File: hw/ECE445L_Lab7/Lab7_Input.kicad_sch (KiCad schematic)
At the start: 5 parts, among them SW1 UP, SW2 DOWN, SW3 LEFT, SW4 RIGHT, SW5 MODE

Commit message: work on schem
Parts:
- removed SW1: UP, ECE445L:SW_PUSH_6mm, symbol ECE445L:SW_Push
- removed SW2: DOWN, ECE445L:SW_PUSH_6mm, symbol ECE445L:SW_Push
- removed SW3: LEFT, ECE445L:SW_PUSH_6mm, symbol ECE445L:SW_Push
- removed SW4: RIGHT, ECE445L:SW_PUSH_6mm, symbol ECE445L:SW_Push
- removed SW5: MODE, ECE445L:SW_PUSH_6mm, symbol ECE445L:SW_Push
- added J2: Conn_01x08, symbol Connector_Generic:Conn_01x08
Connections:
- new net uC_{1} - PA0: J2.5 (Pin_5)
- new net uC_{1} - PA1: J2.6 (Pin_6)
- new net uC_{1} - PA11: J2.8 (Pin_8)
- new net uC_{1} - PA23: J2.3 (Pin_3)
- new net uC_{1} - PA26: J2.4 (Pin_4)
- new net uC_{1} - PA3: J2.7 (Pin_7)
- new net uC_{1} - PA4: J2.1 (Pin_1)
- new net uC_{1} - PA7: J2.2 (Pin_2)

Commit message: more updates
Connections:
- net uC_{1} - PA0 renamed uC_{1} - KC1
- net uC_{1} - PA1 renamed uC_{1} - KC2
- net uC_{1} - PA26 renamed uC_{1} - KR4
- net uC_{1} - PA4 renamed uC_{1} - KR1
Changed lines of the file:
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@@
 	(generator_version "10.0")
 	(paper "A4")
-	(global_label "uC_{1} - PA4"
+	(global_label "uC_{1} - KR1"
 		(shape output)
 		(at 87.63 40.005 180)
@@
 		)
 		(property "Intersheetrefs" "${INTERSHEET_REFS}"
-			(at 74.1825 40.005 0)
+			(at 74.0011 40.005 0)
 			(hide yes)
 			(show_name no)
@@
 		)
 	)
-	(global_label "uC_{1} - PA1"
+	(global_label "uC_{1} - KC2"
 		(shape input)
 		(at 87.63 52.705 180)
@@
 		)
 		(property "Intersheetrefs" "${INTERSHEET_REFS}"
-			(at 74.1825 52.705 0)
+			(at 74.0011 52.705 0)
 			(hide yes)
 			(show_name no)
@@
 		)
 	)
-	(global_label "uC_{1} - PA0"
+	(global_label "uC_{1} - KC1"
 		(shape input)
 		(at 87.63 50.165 180)
@@
 		)
 		(property "Intersheetrefs" "${INTERSHEET_REFS}"
-			(at 74.1825 50.165 0)
+			(at 74.0011 50.165 0)
 			(hide yes)
 			(show_name no)
@@
 		)
 	)
-	(global_label "uC_{1} - PA26"
+	(global_label "uC_{1} - KR4"
 		(shape output)
 		(at 87.63 47.625 180)
@@
 		)
 		(property "Intersheetrefs" "${INTERSHEET_REFS}"
-			(at 72.973 47.625 0)
+			(at 74.0011 47.625 0)
 			(hide yes)
 			(show_name no)

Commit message: mostly finished schem
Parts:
- J_{Keypad}: renamed from J2; footprint (none) -> Connector_PinSocket_2.54mm:PinSocket_1x08_P2.54mm_Vertical
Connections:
- net uC_{1} - PA11 renamed uC_{1} - KC4
- net uC_{1} - PA23 renamed uC_{1} - KR3
- net uC_{1} - PA3 renamed uC_{1} - KC3
- net uC_{1} - PA7 renamed uC_{1} - KR2
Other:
- note added: "ID Reader"
- note added: "Keypad"
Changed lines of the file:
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@@
 	(generator_version "10.0")
 	(paper "A4")
+	(rectangle
+		(start 69.85 34.925)
+		(end 109.855 65.405)
+		(stroke
+			(width 0)
+			(type default)
+		)
+		(fill
+			(type none)
+		)
+	)
+	(rectangle
+		(start 112.395 34.925)
+		(end 152.4 65.405)
+		(stroke
+			(width 0)
+			(type default)
+		)
+		(fill
+			(type none)
+		)
+	)
+	(text "ID Reader"
+		(exclude_from_sim no)
+		(at 146.685 63.5 0)
+		(effects
+			(font
+				(size 1.27 1.27)
+			)
+		)
+	)
+	(text "Keypad"
+		(exclude_from_sim no)
+		(at 105.41 63.5 0)
+		(effects
+			(font
+				(size 1.27 1.27)
+			)
+		)
+	)
 	(global_label "uC_{1} - KR1"
 		(shape output)
@@
 		)
 	)
-	(global_label "uC_{1} - PA23"
+	(global_label "uC_{1} - KR3"
 		(shape output)
 		(at 87.63 45.085 180)
@@
 		)
 		(property "Intersheetrefs" "${INTERSHEET_REFS}"
-			(at 72.973 45.085 0)
-			(hide yes)
-			(show_name no)
-			(do_not_autoplace no)
-			(effects
-				(font
-					(size 1.27 1.27)
-				)
-				(justify right)
-			)
-		)
-	)
-	(global_label "uC_{1} - PA11"
+			(at 74.0011 45.085 0)
+			(hide yes)
+			(show_name no)
+			(do_not_autoplace no)
+			(effects
+				(font
+					(size 1.27 1.27)
+				)
+				(justify right)
+			)
+		)
+	)
+	(global_label "uC_{1} - KC4"
 		(shape input)
 		(at 87.63 57.785 180)
@@
 		)
 		(property "Intersheetrefs" "${INTERSHEET_REFS}"
-			(at 72.973 57.785 0)
+			(at 74.0011 57.785 0)
 			(hide yes)
 			(show_name no)
@@
 		)
 	)
-	(global_label "uC_{1} - PA7"
+	(global_label "uC_{1} - KR2"
 		(shape output)
 		(at 87.63 42.545 180)
@@
 		)
 		(property "Intersheetrefs" "${INTERSHEET_REFS}"
-			(at 74.1825 42.545 0)
+			(at 74.0011 42.545 0)
 			(hide yes)
 			(show_name no)
@@
 		)
 	)
-	(global_label "uC_{1} - PA3"
+	(global_label "uC_{1} - KC3"
 		(shape input)
 		(at 87.63 55.245 180)
@@
 		)
 		(property "Intersheetrefs" "${INTERSHEET_REFS}"
-			(at 74.1825 55.245 0)
+			(at 74.0011 55.245 0)
 			(hide yes)
 			(show_name no)
@@
 		(dnp no)
 		(fields_autoplaced yes)
-		(property "Reference" "J2"
+		(property "Reference" "J_{Keypad}"
 			(at 95.885 47.6249 0)
 			(show_name no)
@@
 			)
 		)
-		(property "Footprint" ""
+		(property "Footprint" "Connector_PinSocket_2.54mm:PinSocket_1x08_P2.54mm_Vertical"
 			(at 92.71 47.625 0)
 			(hide yes)
@@
 			(project "ECE445L_Lab7"
 				(path "/69b823fd-c065-40ff-9bb9-c5835555f3eb/e9432827-5ece-4de0-90fe-13c05c5c04a5"
-					(reference "J2")
+					(reference "J_{Keypad}")
 					(unit 1)
 				)

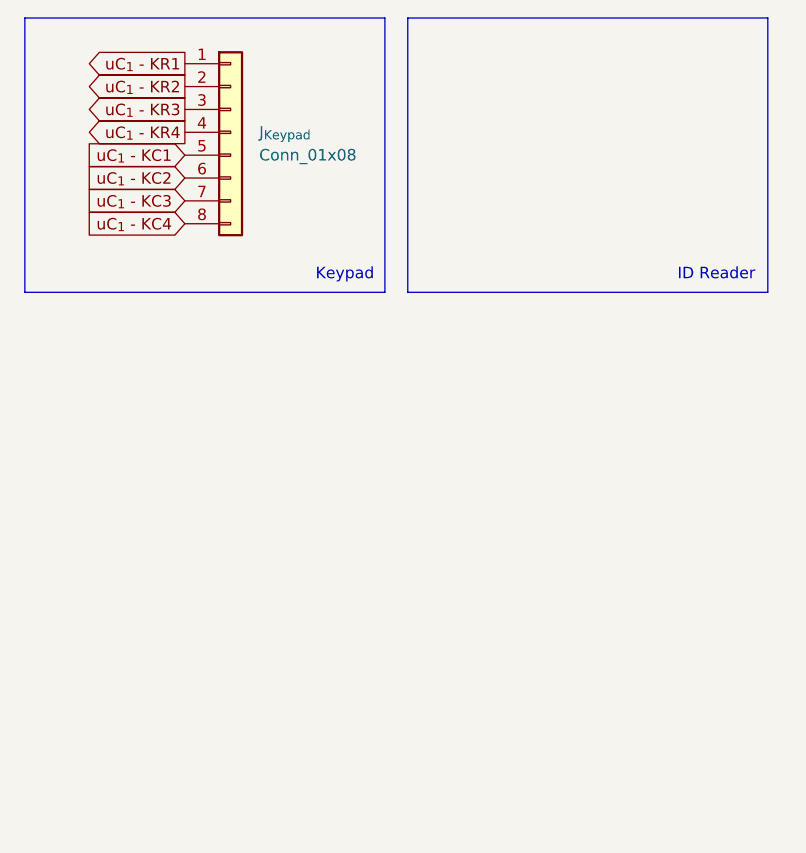
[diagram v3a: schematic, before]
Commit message: added reverse engineering for water atomizer
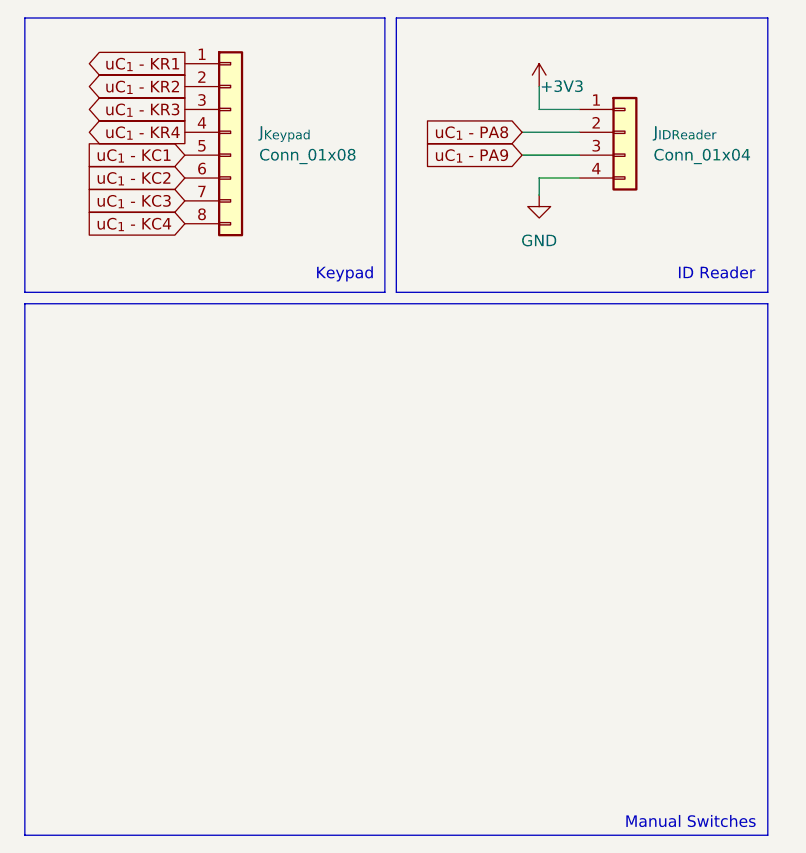
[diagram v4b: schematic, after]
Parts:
- added J_{IDReader}: Conn_01x04, symbol Connector_Generic:Conn_01x04
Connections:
- new net +3V3: J_{IDReader}.1 (Pin_1)
- new net GND: J_{IDReader}.4 (Pin_4)
- new net uC_{1} - PA8: J_{IDReader}.2 (Pin_2)
- new net uC_{1} - PA9: J_{IDReader}.3 (Pin_3)
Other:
- note added: "Manual Switches"
- company: (none) -> ECE445L

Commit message: almost finished with schem
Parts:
- J_{IDReader}: footprint (none) -> Connector_PinSocket_2.54mm:PinSocket_1x04_P2.54mm_Vertical
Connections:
- net uC_{1} - KC1 renamed Keypad - C1
- net uC_{1} - KC2 renamed Keypad - C2
- net uC_{1} - KC3 renamed Keypad - C3
- net uC_{1} - KC4 renamed Keypad - C4
- net uC_{1} - KR1 renamed Keypad - R1
- net uC_{1} - KR2 renamed Keypad - R2
- net uC_{1} - KR3 renamed Keypad - R3
- net uC_{1} - KR4 renamed Keypad - R4
- net uC_{1} - PA8 renamed ID Scan - TxD
- net uC_{1} - PA9 renamed ID Scan - RxD
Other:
- moved on the sheet: J_{Keypad}
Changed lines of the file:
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@@
 	)
 	(rectangle
-		(start 69.85 34.925)
-		(end 109.855 65.405)
+		(start 66.04 34.925)
+		(end 106.045 65.405)
 		(stroke
 			(width 0)
@@
 	)
 	(rectangle
-		(start 111.125 34.925)
+		(start 107.315 34.925)
 		(end 152.4 65.405)
 		(stroke
@@
 	)
 	(rectangle
-		(start 69.85 66.675)
+		(start 66.04 66.675)
 		(end 152.4 125.73)
 		(stroke
@@
 	(text "Keypad"
 		(exclude_from_sim no)
-		(at 105.41 63.5 0)
+		(at 101.6 63.5 0)
 		(effects
 			(font
@@
 		)
 	)
-	(global_label "uC_{1} - KR1"
+	(global_label "Keypad - R1"
 		(shape output)
-		(at 87.63 40.005 180)
-		(fields_autoplaced yes)
-		(effects
-			(font
-				(size 1.27 1.27)
-			)
-			(justify right)
-		)
-		(property "Intersheetrefs" "${INTERSHEET_REFS}"
-			(at 74.0011 40.005 0)
-			(hide yes)
-			(show_name no)
-			(do_not_autoplace no)
-			(effects
-				(font
-					(size 1.27 1.27)
-				)
-				(justify right)
-			)
-		)
-	)
-	(global_label "uC_{1} - PA8"
+		(at 83.82 40.005 180)
+		(fields_autoplaced yes)
+		(effects
+			(font
+				(size 1.27 1.27)
+			)
+			(justify right)
+		)
+		(property "Intersheetrefs" "${INTERSHEET_REFS}"
+			(at 70.1911 40.005 0)
+			(hide yes)
+			(show_name no)
+			(do_not_autoplace no)
+			(effects
+				(font
+					(size 1.27 1.27)
+				)
+				(justify right)
+			)
+		)
+	)
+	(global_label "ID Scan - TxD"
 		(shape input)
 		(at 125.095 47.625 180)
@@
 		)
 	)
-	(global_label "uC_{1} - KR3"
+	(global_label "Keypad - R3"
 		(shape output)
-		(at 87.63 45.085 180)
-		(fields_autoplaced yes)
-		(effects
-			(font
-				(size 1.27 1.27)
-			)
-			(justify right)
-		)
-		(property "Intersheetrefs" "${INTERSHEET_REFS}"
-			(at 74.0011 45.085 0)
-			(hide yes)
-			(show_name no)
-			(do_not_autoplace no)
-			(effects
-				(font
-					(size 1.27 1.27)
-				)
-				(justify right)
-			)
-		)
-	)
-	(global_label "uC_{1} - KC4"
+		(at 83.82 45.085 180)
+		(fields_autoplaced yes)
+		(effects
+			(font
+				(size 1.27 1.27)
+			)
+			(justify right)
+		)
+		(property "Intersheetrefs" "${INTERSHEET_REFS}"
+			(at 70.1911 45.085 0)
+			(hide yes)
+			(show_name no)
+			(do_not_autoplace no)
+			(effects
+				(font
+					(size 1.27 1.27)
+				)
+				(justify right)
+			)
+		)
+	)
+	(global_label "Keypad - C4"
 		(shape input)
-		(at 87.63 57.785 180)
-		(fields_autoplaced yes)
-		(effects
-			(font
-				(size 1.27 1.27)
-			)
-			(justify right)
-		)
-		(property "Intersheetrefs" "${INTERSHEET_REFS}"
-			(at 74.0011 57.785 0)
-			(hide yes)
-			(show_name no)
-			(do_not_autoplace no)
-			(effects
-				(font
-					(size 1.27 1.27)
-				)
-				(justify right)
-			)
-		)
-	)
-	(global_label "uC_{1} - KC2"
+		(at 83.82 57.785 180)
+		(fields_autoplaced yes)
+		(effects
+			(font
+				(size 1.27 1.27)
+			)
+			(justify right)
+		)
+		(property "Intersheetrefs" "${INTERSHEET_REFS}"
+			(at 70.1911 57.785 0)
+			(hide yes)
+			(show_name no)
+			(do_not_autoplace no)
+			(effects
+				(font
+					(size 1.27 1.27)
+				)
+				(justify right)
+			)
+		)
+	)
+	(global_label "Keypad - C2"
 		(shape input)
-		(at 87.63 52.705 180)
-		(fields_autoplaced yes)
-		(effects
-			(font
-				(size 1.27 1.27)
-			)
-			(justify right)
-		)
-		(property "Intersheetrefs" "${INTERSHEET_REFS}"
-			(at 74.0011 52.705 0)
-			(hide yes)
-			(show_name no)
-			(do_not_autoplace no)
-			(effects
-				(font
-					(size 1.27 1.27)
-				)
-				(justify right)
-			)
-		)
-	)
-	(global_label "uC_{1} - KR2"
+		(at 83.82 52.705 180)
+		(fields_autoplaced yes)
+		(effects
+			(font
+				(size 1.27 1.27)
+			)
+			(justify right)
+		)
+		(property "Intersheetrefs" "${INTERSHEET_REFS}"
+			(at 70.1911 52.705 0)
+			(hide yes)
+			(show_name no)
+			(do_not_autoplace no)
+			(effects
+				(font
+					(size 1.27 1.27)
+				)
+				(justify right)
+			)
+		)
+	)
+	(global_label "Keypad - R2"
 		(shape output)
-		(at 87.63 42.545 180)
-		(fields_autoplaced yes)
-		(effects
-			(font
-				(size 1.27 1.27)
-			)
-			(justify right)
-		)
-		(property "Intersheetrefs" "${INTERSHEET_REFS}"
-			(at 74.0011 42.545 0)
-			(hide yes)
-			(show_name no)
-			(do_not_autoplace no)
-			(effects
-				(font
-					(size 1.27 1.27)
-				)
-				(justify right)
-			)
-		)
-	)
-	(global_label "uC_{1} - KC1"
+		(at 83.82 42.545 180)
+		(fields_autoplaced yes)
+		(effects
+			(font
+				(size 1.27 1.27)
+			)
+			(justify right)
+		)
+		(property "Intersheetrefs" "${INTERSHEET_REFS}"
+			(at 70.1911 42.545 0)
+			(hide yes)
+			(show_name no)
+			(do_not_autoplace no)
+			(effects
+				(font
+					(size 1.27 1.27)
+				)
+				(justify right)
+			)
+		)
+	)
+	(global_label "Keypad - C1"
 		(shape input)
-		(at 87.63 50.165 180)
-		(fields_autoplaced yes)
-		(effects
-			(font
-				(size 1.27 1.27)
-			)
-			(justify right)
-		)
-		(property "Intersheetrefs" "${INTERSHEET_REFS}"
-			(at 74.0011 50.165 0)
-			(hide yes)
-			(show_name no)
-			(do_not_autoplace no)
-			(effects
-				(font
-					(size 1.27 1.27)
-				)
-				(justify right)
-			)
-		)
-	)
-	(global_label "uC_{1} - PA9"
+		(at 83.82 50.165 180)
+		(fields_autoplaced yes)
+		(effects
+			(font
+				(size 1.27 1.27)
+			)
+			(justify right)
+		)
+		(property "Intersheetrefs" "${INTERSHEET_REFS}"
+			(at 70.1911 50.165 0)
+			(hide yes)
+			(show_name no)
+			(do_not_autoplace no)
+			(effects
+				(font
+					(size 1.27 1.27)
+				)
+				(justify right)
+			)
+		)
+	)
+	(global_label "ID Scan - RxD"
 		(shape input)
 		(at 125.095 50.165 180)
@@
 		)
 	)
-	(global_label "uC_{1} - KC3"
+	(global_label "Keypad - C3"
 		(shape input)
-		(at 87.63 55.245 180)
-		(fields_autoplaced yes)
-		(effects
-			(font
-				(size 1.27 1.27)
-			)
-			(justify right)
-		)
-		(property "Intersheetrefs" "${INTERSHEET_REFS}"
-			(at 74.0011 55.245 0)
-			(hide yes)
-			(show_name no)
-			(do_not_autoplace no)
-			(effects
-				(font
-					(size 1.27 1.27)
-				)
-				(justify right)
-			)
-		)
-	)
-	(global_label "uC_{1} - KR4"
+		(at 83.82 55.245 180)
+		(fields_autoplaced yes)
+		(effects
+			(font
+				(size 1.27 1.27)
+			)
+			(justify right)
+		)
+		(property "Intersheetrefs" "${INTERSHEET_REFS}"
+			(at 70.1911 55.245 0)
+			(hide yes)
+			(show_name no)
+			(do_not_autoplace no)
+			(effects
+				(font
+					(size 1.27 1.27)
+				)
+				(justify right)
+			)
+		)
+	)
+	(global_label "Keypad - R4"
 		(shape output)
-		(at 87.63 47.625 180)
-		(fields_autoplaced yes)
-		(effects
-			(font
-				(size 1.27 1.27)
-			)
-			(justify right)
-		)
-		(property "Intersheetrefs" "${INTERSHEET_REFS}"
-			(at 74.0011 47.625 0)
+		(at 83.82 47.625 180)
+		(fields_autoplaced yes)
+		(effects
+			(font
+				(size 1.27 1.27)
+			)
+			(justify right)
+		)
+		(property "Intersheetrefs" "${INTERSHEET_REFS}"
+			(at 70.1911 47.625 0)
 			(hide yes)
 			(show_name no)
@@
 	(symbol
 		(lib_id "Connector_Generic:Conn_01x08")
-		(at 92.71 47.625 0)
+		(at 88.9 47.625 0)
 		(unit 1)
 		(body_style 1)
@@
 		(fields_autoplaced yes)
 		(property "Reference" "J_{Keypad}"
-			(at 95.885 47.6249 0)
+			(at 92.075 47.6249 0)
 			(show_name no)
 			(do_not_autoplace no)
@@
 		)
 		(property "Value" "Conn_01x08"
-			(at 95.885 50.1649 0)
+			(at 92.075 50.1649 0)
 			(show_name no)
 			(do_not_autoplace no)
@@
 		)
 		(property "Footprint" "Connector_PinSocket_2.54mm:PinSocket_1x08_P2.54mm_Vertical"
-			(at 92.71 47.625 0)
+			(at 88.9 47.625 0)
 			(hide yes)
 			(show_name no)
@@
 		)
 		(property "Datasheet" ""
-			(at 92.71 47.625 0)
+			(at 88.9 47.625 0)
 			(hide yes)
 			(show_name no)
@@
 		)
 		(property "Description" "Generic connector, single row, 01x08, script generated (kicad-library-utils/schlib/autogen/connector/)"
-			(at 92.71 47.625 0)
+			(at 88.9 47.625 0)
 			(hide yes)
 			(show_name no)
@@
 			)
 		)
-		(property "Footprint" ""
+		(property "Footprint" "Connector_PinSocket_2.54mm:PinSocket_1x04_P2.54mm_Vertical"
 			(at 136.525 47.625 0)
 			(hide yes)

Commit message: finished prelim schem
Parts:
- added D_{flyback}16, D_{flyback}17: 1N914, Diode_THT:D_5W_P12.70mm_Horizontal, symbol Device:D_Small
- added JP_{Motor}1, JP_{Motor}2, JP_{Motor}3, JP_{Motor}4: Jumper_3_Open, Connector_PinHeader_2.54mm:PinHeader_1x03_P2.54mm_Vertical, symbol Jumper:Jumper_3_Open
- added J_{PA14,LED}1, J_{PA21,LED}1, J_{PA3,LED}1, J_{PA7,LED}1: Conn_01x02, Connector_PinSocket_2.54mm:PinSocket_1x02_P2.54mm_Vertical, symbol Connector_Generic:Conn_01x02
- added J_{atomizer}1: Conn_01x03, Connector_PinSocket_2.54mm:PinSocket_1x03_P2.54mm_Vertical, symbol Connector_Generic:Conn_01x03
- added LS1, LS2: Speaker, ECE445L:PinHeader_1x02_P2.54mm_Vertical, symbol ECE445L:Speaker
- added Q16, Q17: NTR4501NT1G, ECE445L:SOT96P237X111-3N, symbol ECE445L:NTR4501NT1G
- added R_{PU}2: 10k, Resistor_SMD:R_0805_2012Metric_Pad1.20x1.40mm_HandSolder, symbol ECE445L:R_0.125W
- added RxD_{ID}1, TxD_{ID}1: TestPoint, TestPoint:TestPoint_Keystone_5010-5014_Multipurpose, symbol Connector:TestPoint
- added TFT1: Adafruit ST7735R, ECE445L:adafruit_st7735r2, symbol ECE445L:Adafruit_ST7735R
- added TFT2: HiLetGo_ST7735R, ECE445L:hiletgo_st7735r2, symbol ECE445L:HiLetGo_ST7735R
- added U_{Decoder}1: MC14514BDWR2G, ECE445L:SOIC-24WB_ONS, symbol ECE445L:MC14514BDWR2G
- J_{Keypad}1: renamed from J_{Keypad}; footprint Connector_PinSocket_2.54mm:PinSocket_1x08_P2.54mm_Vertical -> ECE445L:4x4_Matrix_Keypad
- renumbered J_{IDReader} to J_{IDReader}1
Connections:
- net +3V3: now also D_{flyback}16.1 (K), D_{flyback}17.1 (K), J_{atomizer}1.2 (Pin_2), LS1.1, LS2.1, R_{PU}2.1, TFT1.10 (LITE), TFT1.2 (VCC), TFT2.15 (LED+), TFT2.2 (VCC), U_{Decoder}1.1 (ST), U_{Decoder}1.24 (VDD)
- net GND: now also J_{PA14,LED}1.2 (Pin_2), J_{PA21,LED}1.2 (Pin_2), J_{PA3,LED}1.2 (Pin_2), J_{PA7,LED}1.2 (Pin_2), J_{atomizer}1.3 (Pin_3), Q16.2 (S), Q17.2 (S), TFT1.1 (GND), TFT2.1 (GND), TFT2.16 (LED-), U_{Decoder}1.12 (VSS)
- net ID Scan - RxD: now also RxD_{ID}1.1
- net ID Scan - TxD: now also TxD_{ID}1.1
- new net: D_{flyback}17.2 (A), LS2.2, Q17.3 (D)
- new net: D_{flyback}16.2 (A), LS1.2, Q16.3 (D)
- new net Adafruit - CS: TFT1.6 (TFT_CS)
- new net Adafruit - D/C: TFT1.4 (D/C)
- new net Adafruit - MOSI: TFT1.7 (MOSI)
- new net Adafruit - RST: TFT1.3 (RESET)
- new net Adafruit - SCK: TFT1.8 (SCK)
- new net D_{Motor}1: JP_{Motor}1.3 (B), U_{Decoder}1.2 (D1)
- new net D_{Motor}2: JP_{Motor}2.3 (B), U_{Decoder}1.3 (D2)
- new net D_{Motor}3: JP_{Motor}3.3 (B), U_{Decoder}1.21 (D3)
- new net D_{Motor}4: JP_{Motor}4.3 (B), U_{Decoder}1.22 (D4)
- new net HLG SDC - CS: TFT2.14 (SDC_CS)
- new net HLG SDC - MISO: TFT2.12 (SDC_MISO)
- new net HLG Screen - CS: TFT2.10 (TFT_CS)
- new net HLG Screen - D/C: TFT2.7 (TFTDC)
- new net HLG Screen - MOSI: TFT2.13 (SDC_MOSI), TFT2.8 (TFTMOSI)
- new net HLG Screen- RST: TFT2.6 (RESET)
- new net HiLetGo - SCK: TFT2.11 (SDCSCK), TFT2.9 (TFTSCK)
- new net Motor PWM: R_{PU}2.2, U_{Decoder}1.23 (INH)
- new net Motor_{10}: U_{Decoder}1.20 (S10)
- new net Motor_{11}: U_{Decoder}1.19 (S11)
- new net Motor_{12}: U_{Decoder}1.14 (S12)
- new net Motor_{1}: JP_{Motor}1.1 (A), U_{Decoder}1.9 (S1)
- new net Motor_{2}: JP_{Motor}2.1 (A), U_{Decoder}1.10 (S2)
- new net Motor_{3}: JP_{Motor}3.1 (A), U_{Decoder}1.8 (S3)
- new net Motor_{4}: JP_{Motor}4.1 (A), U_{Decoder}1.7 (S4)
- new net Motor_{5}: U_{Decoder}1.6 (S5)
- new net Motor_{6}: U_{Decoder}1.5 (S6)
- new net Motor_{7}: U_{Decoder}1.4 (S7)
- new net Motor_{8}: U_{Decoder}1.18 (S8)
- new net Motor_{9}: U_{Decoder}1.17 (S9)
- new net PA14/LG3: J_{PA14,LED}1.1 (Pin_1)
- new net PA21/LG4: J_{PA21,LED}1.1 (Pin_1)
- new net PA3/LG1: J_{PA3,LED}1.1 (Pin_1)
- new net PA7/LG2: J_{PA7,LED}1.1 (Pin_1)
- new net Smoke: J_{atomizer}1.1 (Pin_1)
- new net uC_{1} - Speaker: Q16.1 (G)
- new net uC_{2} - Motor_{1}: JP_{Motor}1.2 (C)
- new net uC_{2} - Motor_{2}: JP_{Motor}2.2 (C)
- new net uC_{2} - Motor_{3}: JP_{Motor}3.2 (C)
- new net uC_{2} - Motor_{4}: JP_{Motor}4.2 (C)
- new net uC_{2} - Speaker: Q17.1 (G)
- no-connect marks 0 -> 6
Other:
- note added: "Misc. Outputs"
- note added: "Motor Signal Decoder"
- note added: "Screens"
- note added: "Speakers"
- note added: "Switches/Jumpers"
- note added: "Test Points"
- note removed: "Manual Switches"
- moved on the sheet: J_{IDReader}1, J_{Keypad}1
